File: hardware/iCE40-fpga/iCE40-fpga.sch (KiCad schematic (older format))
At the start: 47 parts, among them J1 USB_B_Micro, J2 JST_PH, J3 Feather, Q1 DMP2045U, U1 MCP73831-2-OT, U2 W25Q32JVZP, U3 AP2112K-3.3, U5 AP2112K-1.2, U6 ICE40UP5K-SG48ITR, X1 DSC6101CI1A

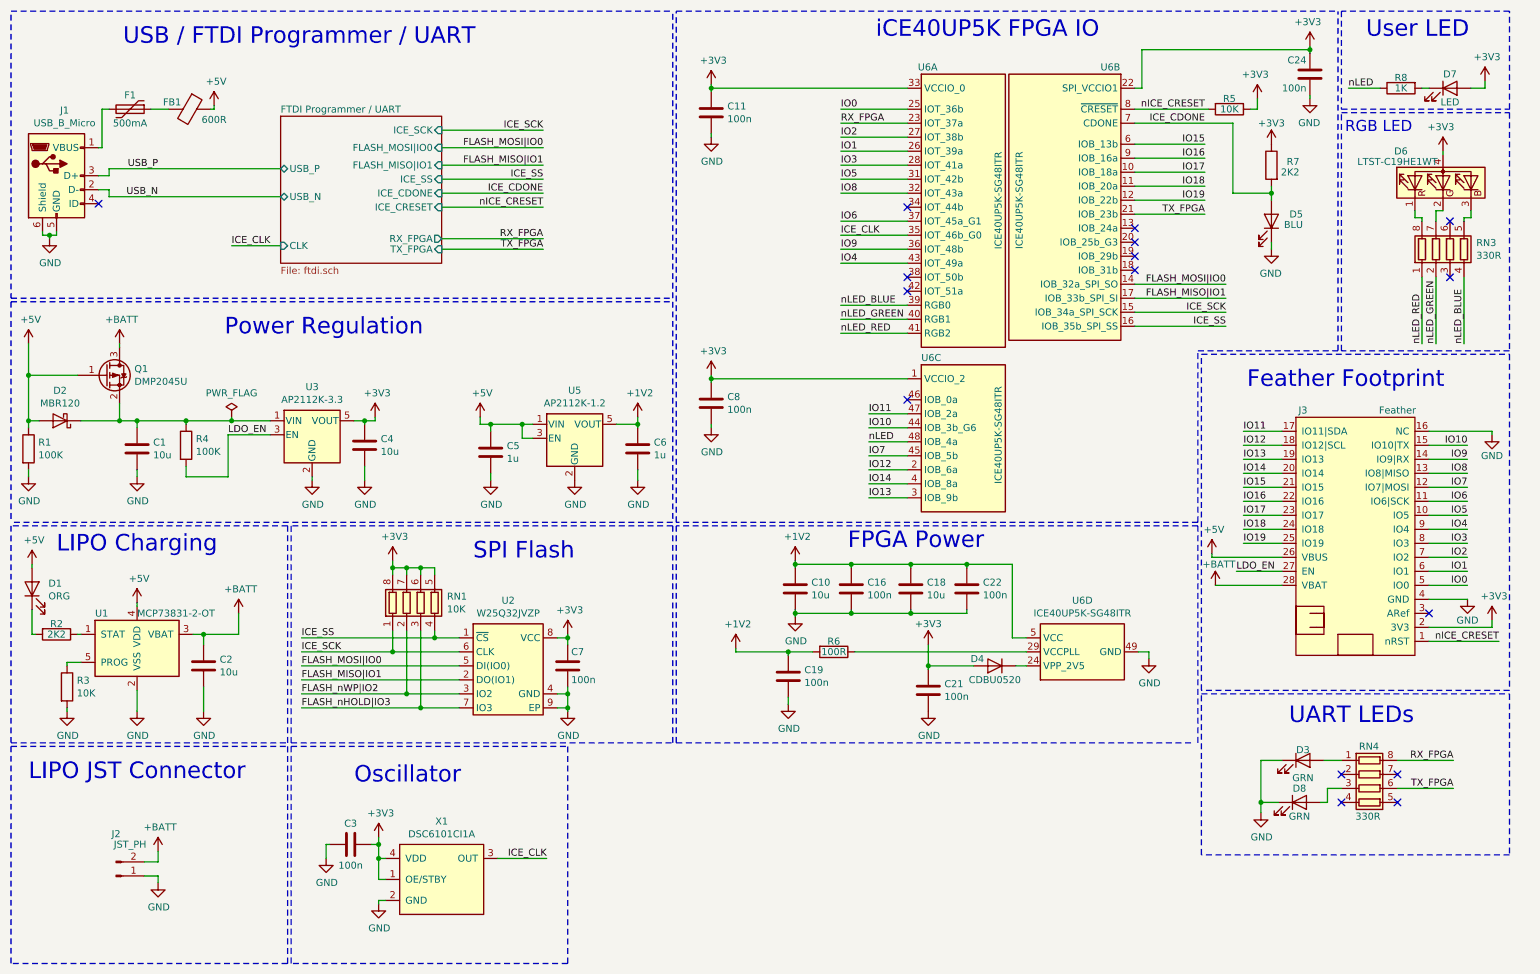
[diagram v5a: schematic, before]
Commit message: changes to make everything work with new library setup
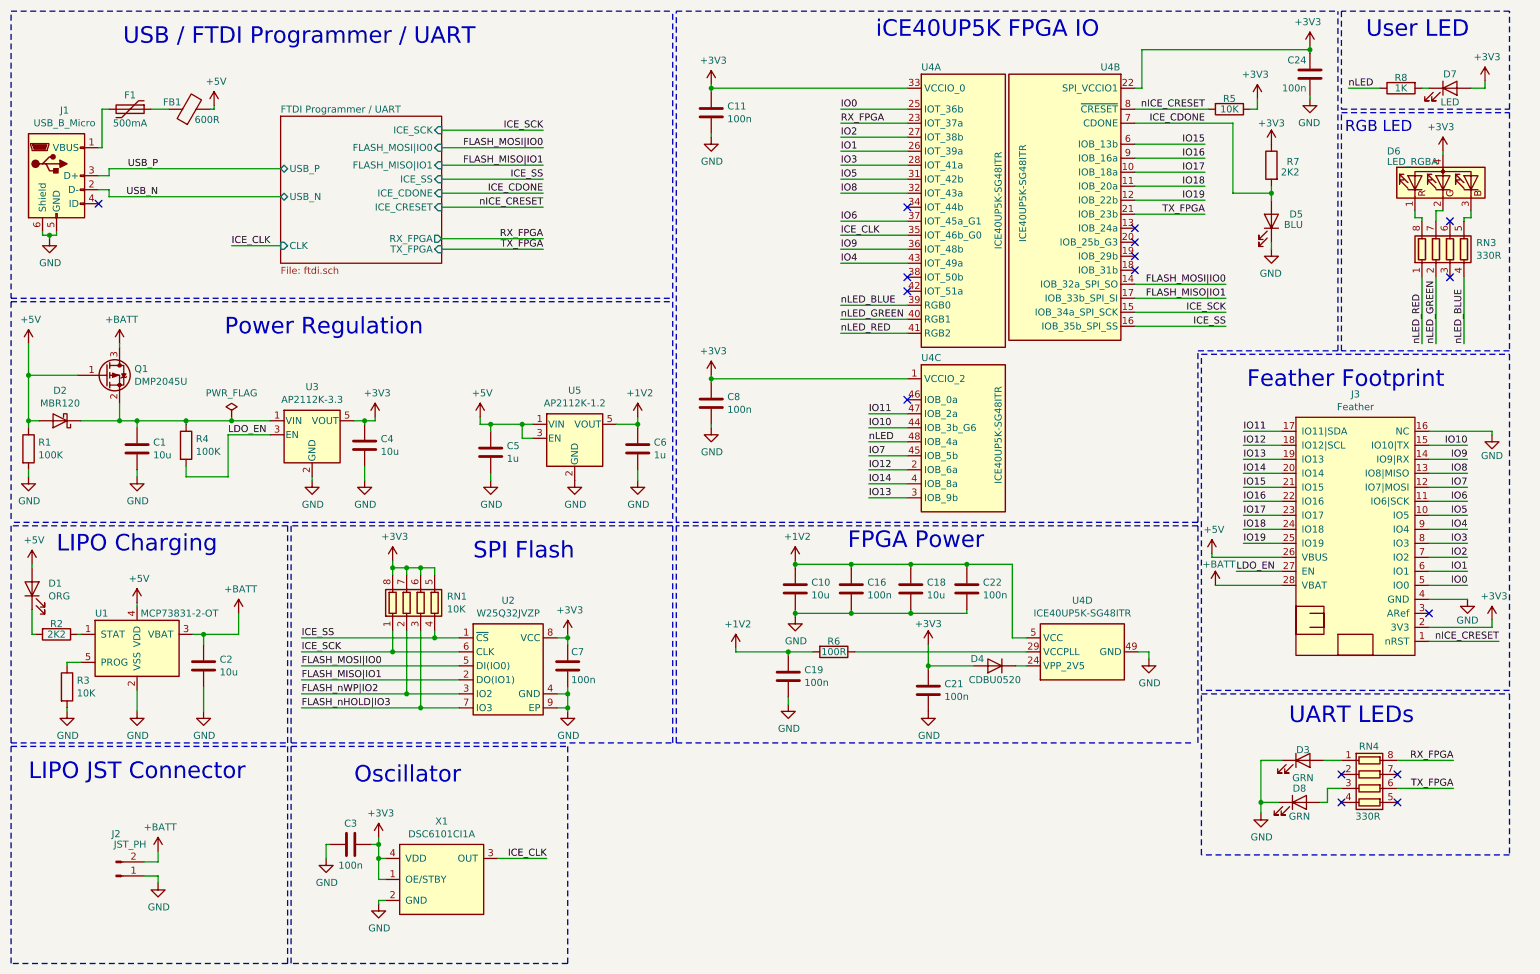
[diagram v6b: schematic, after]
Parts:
- removed D6: LTST-C19HE1WT, josh-footprints:0606LED, symbol josh-symbols:LED_RGBA
- removed FB1: 600R, josh-footprints:BEADC1608X95N, symbol josh-symbols:Ferrite_Bead_PWR
- removed J3: Feather, josh-footprints:PCB_FeatherWing, symbol iCE40-fpga-rescue:Feather-josh-symbols
- removed U1: MCP73831-2-OT, Package_TO_SOT_SMD:SOT-23-5, symbol josh-symbols:MCP73831-2-OT
- removed U2: W25Q32JVZP, josh-footprints:WSON-8-1EP_6x5mm_P1.27mm_EP3.4x4.3mm, symbol josh-symbols:W25Q32JVZP
- removed U6: ICE40UP5K-SG48ITR, josh-footprints:QFN-48-1EP_7x7mm_P0.5mm_EP5.3x5.3mm_ThermalVias, symbol josh-symbols:ICE40UP5K-SG48ITR
- removed X1: DSC6101CI1A, josh-footprints:CDFN_3.2x2.5mm_XO, symbol josh-symbols:DSC6101CI1A
- added D6: LED_RGBA, josh-led:LED_0606, symbol josh-led:LED_RGBA
- added FB1: 600R, josh-passives-smt:Ferrite_Bead_0603, symbol josh-passive:Ferrite_Bead_PWR
- added J3: Feather, josh-connectors:featherwing, symbol josh-mechnanical:Feather
- added U1: MCP73831-2-OT, Package_TO_SOT_SMD:SOT-23-5, symbol josh-power:MCP73831-2-OT
- added U2: W25Q32JVZP, josh-soic-sot-etc:WSON-8-1EP_6x5mm_P1.27mm_EP3.4x4.3mm, symbol josh-memory:W25Q32JVZP
- added U4: ICE40UP5K-SG48ITR, josh-dfn-qfn:QFN-48-1EP_7x7mm_P0.5mm_EP5.3x5.3mm_ThermalVias, symbol josh-ic:ICE40UP5K-SG48ITR
- added X1: DSC6101CI1A, josh-oscillators:CDFN_3.2x2.5mm_XO, symbol josh-oscillator:DSC6101CI1A
- F1: footprint josh-footprints:Fuse_0805_2012Metric -> josh-passives-smt:Fuse_0805_2012Metric
- J1: footprint josh-footprints:MicroUSB_Aliexpress -> josh-connectors:USB_Micro_Aliexpress
- J2: footprint josh-footprints:JST_PH_S2B-PH-SM4-TB_1x02-1MP_P2.00mm_Horizontal -> josh-connectors:JST_PH_S2B-PH-SM4-TB_1x02-1MP_P2.00mm_Horizontal
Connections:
- net +1V2: now also U4.30 (VCC), U4.5 (VCC)
- net +3V3: now also D6.4 (A), J3.2 (3V3), U2.8 (VCC), U4.1 (VCCIO_2), U4.22 (SPI_VCCIO1), U4.33 (VCCIO_0), X1.1 (OE/STBY), X1.4 (VDD)
- net +5V: now also FB1.2, J3.26 (VBUS), U1.4 (VDD)
- net +BATT: now also J3.28 (VBAT), U1.3 (VBAT)
- net FLASH_MISO|IO1: now also U2.2 (DO(IO1)), U4.17 (IOB_33b_SPI_SI)
- net FLASH_MOSI|IO0: now also U2.5 (DI(IO0)), U4.14 (IOB_32a_SPI_SO)
- net FLASH_nHOLD|IO3: now also U2.7 (IO3)
- net FLASH_nWP|IO2: now also U2.3 (IO2)
- net GND: now also J3.16 (NC), J3.4 (GND), U1.2 (VSS), U2.4 (GND), U2.9 (EP), U4.49 (GND), X1.2 (GND)
- net ICE_CDONE: now also U4.7 (CDONE)
- net ICE_CLK: now also U4.35 (IOT_46b_G0), X1.3 (OUT)
- net ICE_SCK: now also U2.6 (CLK), U4.15 (IOB_34a_SPI_SCK)
- net ICE_SS: now also U2.1 (~CS), U4.16 (IOB_35b_SPI_SS)
- net IO0: now also J3.5 (IO0), U4.25 (IOT_36b)
- net IO1: now also J3.6 (IO1), U4.26 (IOT_39a)
- net IO10: now also J3.15 (IO10|TX), U4.44 (IOB_3b_G6)
- net IO11: now also J3.17 (IO11|SDA), U4.47 (IOB_2a)
- net IO12: now also J3.18 (IO12|SCL), U4.2 (IOB_6a)
- net IO13: now also J3.19 (IO13), U4.3 (IOB_9b)
- net IO14: now also J3.20 (IO14), U4.4 (IOB_8a)
- net IO15: now also J3.21 (IO15), U4.6 (IOB_13b)
- net IO16: now also J3.22 (IO16), U4.9 (IOB_16a)
- net IO17: now also J3.23 (IO17), U4.10 (IOB_18a)
- net IO18: now also J3.24 (IO18), U4.11 (IOB_20a)
- net IO19: now also J3.25 (IO19), U4.12 (IOB_22b)
- net IO2: now also J3.7 (IO2), U4.27 (IOT_38b)
- net IO3: now also J3.8 (IO3), U4.28 (IOT_41a)
- net IO4: now also J3.9 (IO4), U4.43 (IOT_49a)
- net IO5: now also J3.10 (IO5), U4.31 (IOT_42b)
- net IO6: now also J3.11 (IO6|SCK), U4.37 (IOT_45a_G1)
- net IO7: now also J3.12 (IO7|MOSI), U4.45 (IOB_5b)
- net IO8: now also J3.13 (IO8|MISO), U4.32 (IOT_43a)
- net IO9: now also J3.14 (IO9|RX), U4.36 (IOT_48b)
- net LDO_EN: now also J3.27 (EN)
- net RX_FPGA: now also U4.23 (IOT_37a)
- net TX_FPGA: now also U4.21 (IOB_23b)
- net nICE_CRESET: now also J3.1 (nRST), U4.8 (~CRESET)
- net nLED: now also U4.48 (IOB_4a)
- net nLED_BLUE: now also U4.39 (RGB0)
- net nLED_GREEN: now also U4.40 (RGB1)
- net nLED_RED: now also U4.41 (RGB2)
- net at F1.1: now also FB1.1
- net at RN3.5 (R4.2): now also D6.3 (BK)
- net at RN3.7 (R2.2): now also D6.2 (GK)
- net at RN3.8 (R1.2): now also D6.1 (RK)
- net at D4.1 (K): now also U4.24 (VPP_2V5)
- net at R6.1: now also U4.29 (VCCPLL)
- net at R3.1: now also U1.5 (PROG)
- net at R2.1: now also U1.1 (STAT)
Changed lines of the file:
@@
 F 0 "J1" H 882 2142 50  0000 C CNN
 F 1 "USB_B_Micro" H 882 2051 50  0000 C CNN
-F 2 "josh-footprints:MicroUSB_Aliexpress" H 975 1625 50  0001 C CNN
+F 2 "josh-connectors:USB_Micro_Aliexpress" H 975 1625 50  0001 C CNN
 F 3 "~" H 975 1625 50  0001 C CNN
 	1    825  1675
@@
 Wire Wire Line
 	5675 5050 5675 5075
-$Comp
-L josh-symbols:ICE40UP5K-SG48ITR U6
-U 4 1 5D7B18BA
-P 8150 5075
-F 0 "U6" V 8517 5075 50  0000 C CNN
-F 1 "ICE40UP5K-SG48ITR" V 8426 5075 50  0000 C CNN
-F 2 "josh-footprints:QFN-48-1EP_7x7mm_P0.5mm_EP5.3x5.3mm_ThermalVias" H 8150 3725 50  0001 C CNN
-F 3 "http://www.latticesemi.com/Products/FPGAandCPLD/iCE40Ultra" H 7750 6075 50  0001 C CNN
-	4    8150 5075
-	0    -1   -1   0
-$EndComp
 Wire Wire Line
 	6525 5075 7750 5075
@@
 Wire Notes Line
 	8975 4175 5250 4175
-$Comp
-L josh-symbols:LED_RGBA D6
-U 1 1 5DF3E79D
-P 10725 1725
-F 0 "D6" V 10950 2025 50  0000 C CNN
-F 1 "LTST-C19HE1WT" V 10875 2050 50  0000 C CNN
-F 2 "josh-footprints:0606LED" H 10725 1675 50  0001 C CNN
-F 3 "~" H 10725 1675 50  0001 C CNN
-	1    10725 1725
-	0    -1   -1   0
-$EndComp
 $Comp
 L power:+3V3 #PWR050
@@
 	1    0    0    -1
 $EndComp
-$Comp
-L josh-symbols:DSC6101CI1A X1
-U 1 1 5D21E955
-P 3575 6700
-F 0 "X1" H 3575 7115 50  0000 C CNN
-F 1 "DSC6101CI1A" H 3575 7024 50  0000 C CNN
-F 2 "josh-footprints:CDFN_3.2x2.5mm_XO" H 3475 7300 100 0001 C CNN
-F 3 "" H 3475 7300 100 0001 C CNN
-F 4 "DSC6101CI1A-012.0000T" H 3475 7300 100 0001 C CNN "MPN"
-	1    3575 6700
-	1    0    0    -1
-$EndComp
-$Comp
-L josh-symbols:ICE40UP5K-SG48ITR U6
-U 1 1 5D956843
-P 7300 1800
-F 0 "U6" H 6975 2700 50  0000 L CNN
-F 1 "ICE40UP5K-SG48ITR" V 7550 1400 50  0000 L CNN
-F 2 "josh-footprints:QFN-48-1EP_7x7mm_P0.5mm_EP5.3x5.3mm_ThermalVias" H 7300 450 50  0001 C CNN
-F 3 "http://www.latticesemi.com/Products/FPGAandCPLD/iCE40Ultra" H 6900 2800 50  0001 C CNN
-	1    7300 1800
-	1    0    0    -1
-$EndComp
-$Comp
-L josh-symbols:ICE40UP5K-SG48ITR U6
-U 2 1 5D957FE6
-P 8025 1850
-F 0 "U6" H 7700 2800 50  0000 C CNN
-F 1 "ICE40UP5K-SG48ITR" V 8350 1850 50  0000 C CNN
-F 2 "josh-footprints:QFN-48-1EP_7x7mm_P0.5mm_EP5.3x5.3mm_ThermalVias" H 8025 500 50  0001 C CNN
-F 3 "http://www.latticesemi.com/Products/FPGAandCPLD/iCE40Ultra" H 7625 2850 50  0001 C CNN
-	2    8025 1850
-	-1   0    0    -1
-$EndComp
-$Comp
-L josh-symbols:ICE40UP5K-SG48ITR U6
-U 3 1 5D9593F0
-P 7300 3475
-F 0 "U6" H 7000 3975 50  0000 L CNN
-F 1 "ICE40UP5K-SG48ITR" V 7550 3075 50  0000 L CNN
-F 2 "josh-footprints:QFN-48-1EP_7x7mm_P0.5mm_EP5.3x5.3mm_ThermalVias" H 7300 2125 50  0001 C CNN
-F 3 "http://www.latticesemi.com/Products/FPGAandCPLD/iCE40Ultra" H 6900 4475 50  0001 C CNN
-	3    7300 3475
-	1    0    0    -1
-$EndComp
 Text Notes 6675 700  0    118  ~ 0
 iCE40UP5K FPGA IO
@@
 Wire Notes Line
 	5250 4150 5250 500
-$Comp
-L iCE40-fpga-rescue:Feather-josh-symbols J3
-U 1 1 60FEA732
-P 10075 4200
-F 0 "J3" H 9725 5050 50  0000 C CNN
-F 1 "Feather" H 10400 5050 50  0000 C CNN
-F 2 "josh-footprints:PCB_FeatherWing" H 10075 5150 50  0001 C CNN
-F 3 "" H 10075 5150 50  0001 C CNN
-	1    10075 4200
-	1    0    0    -1
-$EndComp
 Text Notes 9325 3200 0    118  ~ 0
 Feather Footprint
@@
 F 0 "J2" H 1250 6375 50  0000 C CNN
 F 1 "JST_PH" H 1350 6450 50  0000 C CNN
-F 2 "josh-footprints:JST_PH_S2B-PH-SM4-TB_1x02-1MP_P2.00mm_Horizontal" H 1250 6675 50  0001 C CNN
+F 2 "josh-connectors:JST_PH_S2B-PH-SM4-TB_1x02-1MP_P2.00mm_Horizontal" H 1250 6675 50  0001 C CNN
 F 3 "~" H 1250 6675 50  0001 C CNN
 	1    1250 6675
@@
 	1    0    0    -1
 $EndComp
-$Comp
-L josh-symbols:MCP73831-2-OT U1
-U 1 1 61B3FFEE
-P 1400 5050
-F 0 "U1" H 1100 5300 50  0000 L CNN
-F 1 "MCP73831-2-OT" H 1400 5300 50  0000 L CNN
-F 2 "Package_TO_SOT_SMD:SOT-23-5" H 1450 4800 50  0001 L CIN
-F 3 "http://ww1.microchip.com/downloads/en/DeviceDoc/20001984g.pdf" H 1250 5000 50  0001 C CNN
-	1    1400 5050
-	1    0    0    -1
-$EndComp
 Text Notes 625  6000 0    118  ~ 0
 LIPO JST Connector
@@
 	1    0    0    -1
 $EndComp
-$Comp
-L josh-symbols:Ferrite_Bead_PWR FB1
-U 1 1 5D6790C3
-P 1775 1200
-F 0 "FB1" V 1725 1075 50  0000 C CNN
-F 1 "600R " V 1850 1375 50  0000 C CNN
-F 2 "josh-footprints:BEADC1608X95N" V 1705 1200 50  0001 C CNN
-F 3 "~" H 1775 1200 50  0001 C CNN
-	1    1775 1200
-	0    1    1    0
-$EndComp
 Wire Wire Line
 	1150 1200 1150 1475
@@
 F 0 "F1" V 1250 1200 50  0000 C CNN
 F 1 "500mA" V 1450 1200 50  0000 C CNN
-F 2 "josh-footprints:Fuse_0805_2012Metric" H 1400 1000 50  0001 L CNN
+F 2 "josh-passives-smt:Fuse_0805_2012Metric" H 1400 1000 50  0001 L CNN
 F 3 "~" H 1350 1200 50  0001 C CNN
 	1    1350 1200
@@
 Wire Wire Line
 	10575 1975 10575 2000
-Wire Wire Line
-	10725 1925 10675 1925
-Wire Wire Line
-	10675 1925 10675 2000
 Wire Wire Line
 	10925 1975 10925 1925
@@
 	1    9400 1125
 	-1   0    0    -1
-$EndComp
-$Comp
-L josh-symbols:W25Q32JVZP U2
-U 1 1 5D231D5E
-P 4200 5175
-F 0 "U2" H 4050 5642 50  0000 C CNN
-F 1 "W25Q32JVZP" H 4050 5551 50  0000 C CNN
-F 2 "josh-footprints:WSON-8-1EP_6x5mm_P1.27mm_EP3.4x4.3mm" H 4200 5175 50  0001 C CNN
-F 3 "http://www.winbond.com/resource-files/w25q32jv%20revg%2003272018%20plus.pdf" H 4200 5175 50  0001 C CNN
-	1    4200 5175
-	1    0    0    -1
 $EndComp
 Wire Wire Line
@@
 Wire Wire Line
 	3425 5475 3700 5475
+$Comp
+L josh-ic:ICE40UP5K-SG48ITR U4
+U 1 1 5D149515
+P 7300 1800
+F 0 "U4" H 7000 2700 50  0000 L CNN
+F 1 "ICE40UP5K-SG48ITR" V 7550 1400 50  0000 L CNN
+F 2 "josh-dfn-qfn:QFN-48-1EP_7x7mm_P0.5mm_EP5.3x5.3mm_ThermalVias" H 7300 450 50  0001 C CNN
+F 3 "http://www.latticesemi.com/Products/FPGAandCPLD/iCE40Ultra" H 6900 2800 50  0001 C CNN
+	1    7300 1800
+	1    0    0    -1
+$EndComp
+$Comp
+L josh-ic:ICE40UP5K-SG48ITR U4
+U 2 1 5D14A139
+P 8025 1850
+F 0 "U4" H 7700 2800 50  0000 C CNN
+F 1 "ICE40UP5K-SG48ITR" V 8325 1900 50  0000 C CNN
+F 2 "josh-dfn-qfn:QFN-48-1EP_7x7mm_P0.5mm_EP5.3x5.3mm_ThermalVias" H 8025 500 50  0001 C CNN
+F 3 "http://www.latticesemi.com/Products/FPGAandCPLD/iCE40Ultra" H 7625 2850 50  0001 C CNN
+	2    8025 1850
+	-1   0    0    -1
+$EndComp
+$Comp
+L josh-ic:ICE40UP5K-SG48ITR U4
+U 4 1 5D14D4D9
+P 8150 5075
+F 0 "U4" V 8517 5075 50  0000 C CNN
+F 1 "ICE40UP5K-SG48ITR" V 8426 5075 50  0000 C CNN
+F 2 "josh-dfn-qfn:QFN-48-1EP_7x7mm_P0.5mm_EP5.3x5.3mm_ThermalVias" H 8150 3725 50  0001 C CNN
+F 3 "http://www.latticesemi.com/Products/FPGAandCPLD/iCE40Ultra" H 7750 6075 50  0001 C CNN
+	4    8150 5075
+	0    -1   -1   0
+$EndComp
+Wire Wire Line
+	10725 1925 10675 1925
+Wire Wire Line
+	10675 1925 10675 2000
+$Comp
+L josh-ic:ICE40UP5K-SG48ITR U4
+U 3 1 5D14B5D1
+P 7300 3475
+F 0 "U4" H 7000 3975 50  0000 L CNN
+F 1 "ICE40UP5K-SG48ITR" V 7550 3075 50  0000 L CNN
+F 2 "josh-dfn-qfn:QFN-48-1EP_7x7mm_P0.5mm_EP5.3x5.3mm_ThermalVias" H 7300 2125 50  0001 C CNN
+F 3 "http://www.latticesemi.com/Products/FPGAandCPLD/iCE40Ultra" H 6900 4475 50  0001 C CNN
+	3    7300 3475
+	1    0    0    -1
+$EndComp
+$Comp
+L josh-led:LED_RGBA D6
+U 1 1 5D15DF05
+P 10725 1725
+F 0 "D6" V 10950 2125 50  0000 R CNN
+F 1 "LED_RGBA" V 10875 2125 50  0000 R CNN
+F 2 "josh-led:LED_0606" H 10725 1675 50  0001 C CNN
+F 3 "~" H 10725 1675 50  0001 C CNN
+	1    10725 1725
+	0    -1   -1   0
+$EndComp
+$Comp
+L josh-mechnanical:Feather J3
+U 1 1 5D18E7FC
+P 10075 4200
+F 0 "J3" H 10100 5165 50  0000 C CNN
+F 1 "Feather" H 10100 5074 50  0000 C CNN
+F 2 "josh-connectors:featherwing" H 10275 3250 50  0001 C CNN
+F 3 "" H 10275 3250 50  0001 C CNN
+	1    10075 4200
+	1    0    0    -1
+$EndComp
+$Comp
+L josh-power:MCP73831-2-OT U1
+U 1 1 5D1900C1
+P 1400 5050
+F 0 "U1" H 1100 5300 50  0000 L CNN
+F 1 "MCP73831-2-OT" H 1425 5300 50  0000 L CNN
+F 2 "Package_TO_SOT_SMD:SOT-23-5" H 1450 4800 50  0001 L CIN
+F 3 "http://ww1.microchip.com/downloads/en/DeviceDoc/20001984g.pdf" H 1250 5000 50  0001 C CNN
+	1    1400 5050
+	1    0    0    -1
+$EndComp
+$Comp
+L josh-memory:W25Q32JVZP U2
+U 1 1 5D1A5CE7
+P 4200 5175
+F 0 "U2" H 4050 5642 50  0000 C CNN
+F 1 "W25Q32JVZP" H 4050 5551 50  0000 C CNN
+F 2 "josh-soic-sot-etc:WSON-8-1EP_6x5mm_P1.27mm_EP3.4x4.3mm" H 4200 5175 50  0001 C CNN
+F 3 "http://www.winbond.com/resource-files/w25q32jv%20revg%2003272018%20plus.pdf" H 4200 5175 50  0001 C CNN
+	1    4200 5175
+	1    0    0    -1
+$EndComp
+$Comp
+L josh-oscillator:DSC6101CI1A X1
+U 1 1 5D1A645F
+P 3575 6700
+F 0 "X1" H 3575 7115 50  0000 C CNN
+F 1 "DSC6101CI1A" H 3575 7024 50  0000 C CNN
+F 2 "josh-oscillators:CDFN_3.2x2.5mm_XO" H 3475 7300 100 0001 C CNN
+F 3 "" H 3475 7300 100 0001 C CNN
+F 4 "DSC6101CI1A-012.0000T" H 3475 7300 100 0001 C CNN "MPN"
+	1    3575 6700
+	1    0    0    -1
+$EndComp
+$Comp
+L josh-passive:Ferrite_Bead_PWR FB1
+U 1 1 5D168C93
+P 1775 1200
+F 0 "FB1" H 1650 1250 50  0000 C CNN
+F 1 "600R" H 1900 1125 50  0000 C CNN
+F 2 "josh-passives-smt:Ferrite_Bead_0603" H 1775 1130 50  0001 C CNN
+F 3 "~" V 1775 1200 50  0001 C CNN
+	1    1775 1200
+	1    0    0    -1
+$EndComp
 $EndSCHEMATC
